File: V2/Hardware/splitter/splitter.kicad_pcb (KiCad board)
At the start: 2 copper layers, 19 parts, among them J0 Rpi_40Pin_F, J1 Control_seg:1, J2 Control_seg:2, J3 Control_seg:3, J4 Molex_PSU_F, J5 Siren, J6 USB_A_F, K0 RELRAS0515, Q0 BC548C, Q1 BD139-16

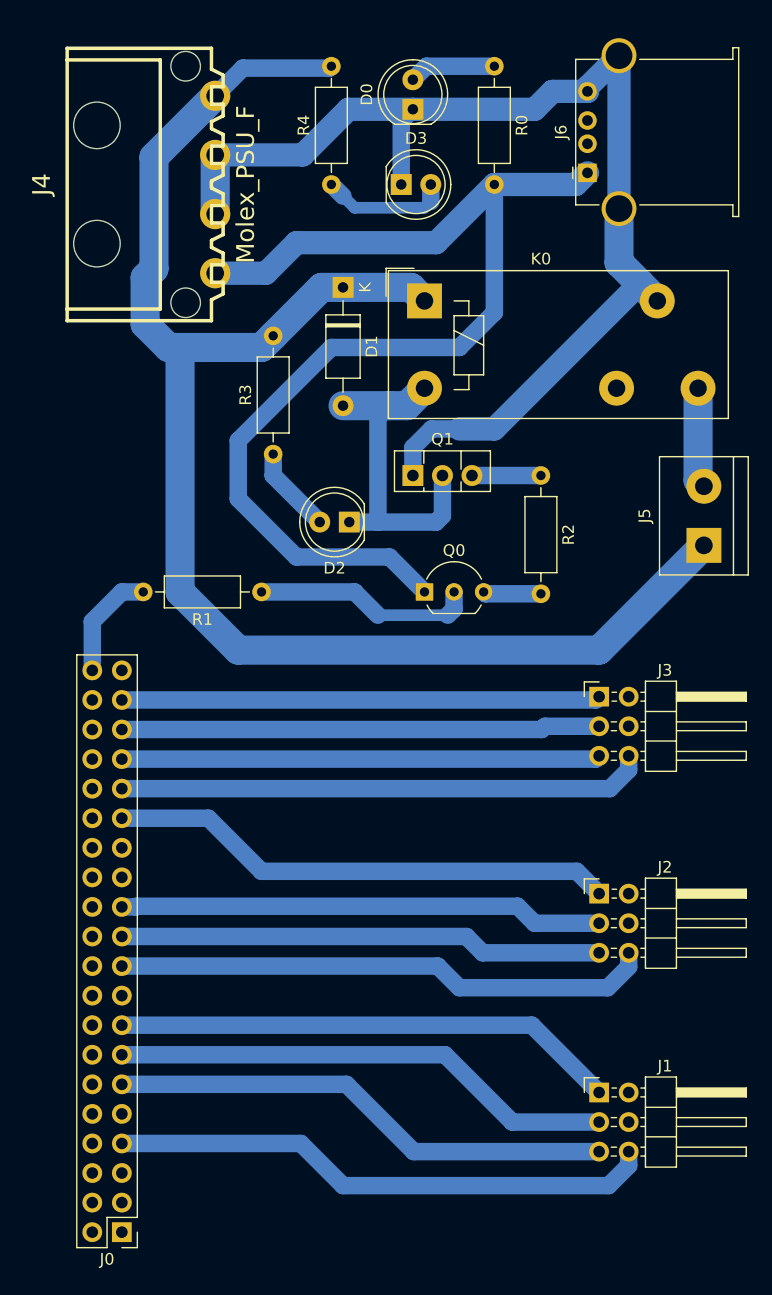
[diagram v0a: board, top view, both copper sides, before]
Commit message: Reinforce output
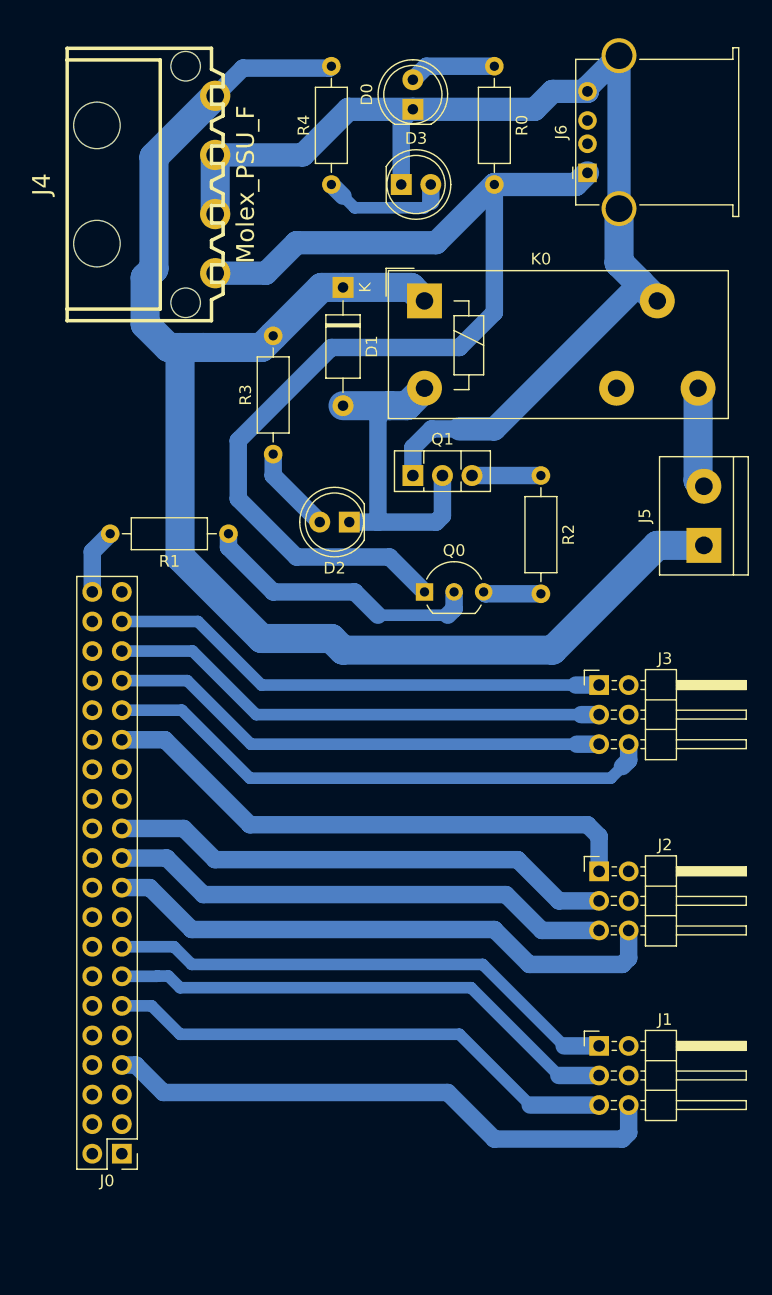
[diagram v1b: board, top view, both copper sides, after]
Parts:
- moved J0 6.74 mm to (124.0, 135.3)
- moved R1 5.75 mm to (133.2, 82.0)
- moved J1 4.00 mm to (165.0, 126.0)
- moved J2 1.92 mm to (165.0, 111.0)
- moved J3 1.00 mm to (165.0, 95.0)
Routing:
- net Net-(Q0-Pad2): track 19.1 -> 24.6 mm
- net /SIREN_gpio:21: track 9.63 -> 5.64 mm
- net /seg:2_bit:d_gpio:05: track 43.7 -> 47.4 mm
- net /seg:2_bit:a_gpio:10: track 46.3 -> 48.9 mm
- net /seg:3_bit:a_gpio:06: track 45.4 -> 48.0 mm
- net /seg:3_bit:c_gpio:19: track 41.1 -> 43.3 mm
- net /seg:3_bit:d_gpio:26: track 41.1 -> 43.3 mm
- net /seg:3_bit:b_gpio:13: track 41.1 -> 43.3 mm
- net /seg:2_bit:b_gpio:09: track 41.6 -> 43.6 mm
- net /seg:2_bit:c_gpio:11: track 41.6 -> 43.6 mm
- net /seg:1_bit:a_gpio:04: track 47.0 -> 48.8 mm
- net /12V+: track 132.4 -> 130.6 mm
- net /seg:1_bit:c_gpio:27: track 43.4 -> 44.5 mm
- net /seg:1_bit:b_gpio:17: track 43.4 -> 44.5 mm
- net /seg:1_bit:d_gpio:22: track 43.4 -> 44.5 mm
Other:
- board text added: "100mm"
- board text removed: "107mm"

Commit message: Export -pcbs
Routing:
- net /seg:3_bit:d_gpio:26: track 43.3 -> 45.7 mm
- net /seg:3_bit:c_gpio:19: track 43.3 -> 45.3 mm
- net (no net): vias 0 -> 7
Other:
- board text added: "RPI"
- board text added: "SEG1"
- board text added: "SEG2"
- board text added: "SEG3"
- board text added: "SIREN"

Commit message: Fix relay symbol
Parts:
- K0: footprint Relay_THT:Relay_SPDT_Finder_40.31 -> Relay_THT:Relay_SPDT_Finder_36.11
- R1: value 100k -> 33k
- moved D1 12.0 mm to (155.0, 59.8)
- moved K0 10.8 mm to (160.0, 66.0)
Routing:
- net /12V+: track 130.6 -> 188.7 mm
- net Net-(J5-Pad2): track 8.63 -> 38.9 mm
- net Net-(D1-Pad2): track 29.7 -> 48.0 mm
- net /5V+: track 97.4 -> 109.7 mm
- net Earth: track 100.6 -> 107.8 mm
- net Net-(K0-Pad12): track 0.00 -> 5.20 mm
- net Net-(Q0-Pad3): track 4.99 -> 7.18 mm
- net Net-(Q1-Pad3): track 5.92 -> 7.92 mm
- net /SIREN_gpio:21: track 5.64 -> 7.64 mm
- net Net-(D0-Pad2): track 7.48 -> 9.32 mm
- net Net-(Q0-Pad2): track 24.6 -> 26.3 mm
- net Net-(D2-Pad2): track 7.50 -> 8.68 mm
- net Net-(D3-Pad2): track 11.1 -> 11.6 mm
- net (no net): vias 7 -> 8

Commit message: Update splitter board
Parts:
- J0: footprint Connector_PinHeader_2.54mm:PinHeader_2x20_P2.54mm_Vertical -> Connector_IDC:IDC-Header_2x20_P2.54mm_Vertical
- moved Q1 10.0 mm to (149.0, 67.0), turned to 270 degrees
- moved R1 9.78 mm to (137.0, 73.0)
- moved Q0 9.30 mm to (152.0, 77.9), turned to 270 degrees
- moved R3 7.91 mm to (143.0, 70.0)
- moved D2 4.47 mm to (145.5, 77.0)
- moved J0 3.05 mm to (124.5, 132.3)
- moved R2 3.00 mm to (157.0, 77.0), turned to 0 degrees
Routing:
- net Earth: track 107.8 -> 95.9 mm
- net /12V+: track 188.7 -> 177.9 mm
- net Net-(Q0-Pad3): track 7.18 -> 17.6 mm
- net /SIREN_gpio:21: track 7.64 -> 16.4 mm
- net /5V+: track 109.7 -> 101.8 mm
- net /seg:3_bit:a_gpio:06: track 48.0 -> 51.9 mm
- net Net-(D1-Pad2): track 48.0 -> 44.8 mm
- net Net-(Q1-Pad3): track 7.92 -> 10.0 mm
- net /seg:3_bit:c_gpio:19: track 45.3 -> 44.0 mm
- net /seg:1_bit:d_gpio:22: track 44.5 -> 45.8 mm
- net /seg:3_bit:b_gpio:13: track 43.3 -> 44.0 mm
- net /seg:2_bit:c_gpio:11: track 43.6 -> 44.3 mm
- net /seg:2_bit:a_gpio:10: track 48.9 -> 49.6 mm
- net /seg:2_bit:b_gpio:09: track 43.6 -> 44.3 mm
- net /seg:1_bit:b_gpio:17: track 44.5 -> 45.2 mm
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
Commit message: Make more precise plots
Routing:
- net (no net): track 0.00 -> 4.00 mm
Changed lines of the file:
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@@
   (general
     (thickness 1.6)
-    (drawings 27)
-    (tracks 224)
+    (drawings 29)
+    (tracks 226)
     (zones 0)
     (modules 19)
@@
   )
   (setup
-    (last_trace_width 2)
+    (last_trace_width 0.25)
     (user_trace_width 1)
     (user_trace_width 1.5)
@@
     (visible_elements FFFFFF7F)
     (pcbplotparams
-      (layerselection 0x010fc_ffffffff)
+      (layerselection 0x00800_fffffffe)
       (usegerberextensions false)
       (usegerberattributes true)
       (usegerberadvancedattributes true)
       (creategerberjobfile true)
-      (excludeedgelayer true)
+      (excludeedgelayer false)
       (linewidth 0.100000)
       (plotframeref false)
@@
       (psnegative false)
       (psa4output false)
-      (plotreference true)
-      (plotvalue true)
+      (plotreference false)
+      (plotvalue false)
       (plotinvisibletext false)
-      (padsonsilk false)
+      (padsonsilk true)
       (subtractmaskfromsilk false)
-      (outputformat 1)
+      (outputformat 5)
       (mirror false)
       (drillshape 1)
@@
     (pad 3 thru_hole circle (at 0 2.54 180) (size 1.7 1.7) (drill 1) (layers *.Cu *.Mask)
       (net 9 "Net-(J0-Pad3)"))
-    (pad 1 thru_hole roundrect (at 0 0 180) (size 1.7 1.7) (drill 1) (layers *.Cu *.Mask) (roundrect_rratio 0.147059)
+    (pad 1 thru_hole roundrect (at 0 0 180) (size 1.7 1.7) (drill 1) (layers *.Cu *.Mask) (roundrect_rratio 0.1470588235294118)
       (net 7 "Net-(J0-Pad1)"))
     (model ${KISYS3DMOD}/Connector_IDC.3dshapes/IDC-Header_2x20_P2.54mm_Vertical.wrl
@@
     )
   )
+  (gr_line (start 141 132) (end 139 132) (layer Eco2.User) (width 0.25))
+  (gr_line (start 140 131) (end 140 133) (layer Eco2.User) (width 0.25))
   (gr_circle (center 136 54) (end 137 55) (layer Eco2.User) (width 0.15))
   (gr_circle (center 136 54) (end 137 53) (layer F.CrtYd) (width 0.05))
@@
   (via (at 160 41) (size 0.8) (drill 0.4) (layers F.Cu B.Cu) (net 0))
   (via (at 136 54) (size 0.8) (drill 0.4) (layers F.Cu B.Cu) (net 0))
+  (segment (start 140 131) (end 140 133) (width 0.25) (layer B.Cu) (net 0))
+  (segment (start 141 132) (end 139 132) (width 0.25) (layer B.Cu) (net 0))
   (segment (start 132.02 49.46) (end 132.02 54.54) (width 2.5) (layer B.Cu) (net 1))
   (segment (start 148 46.54) (end 149 45.54) (width 1.5) (layer B.Cu) (net 1))

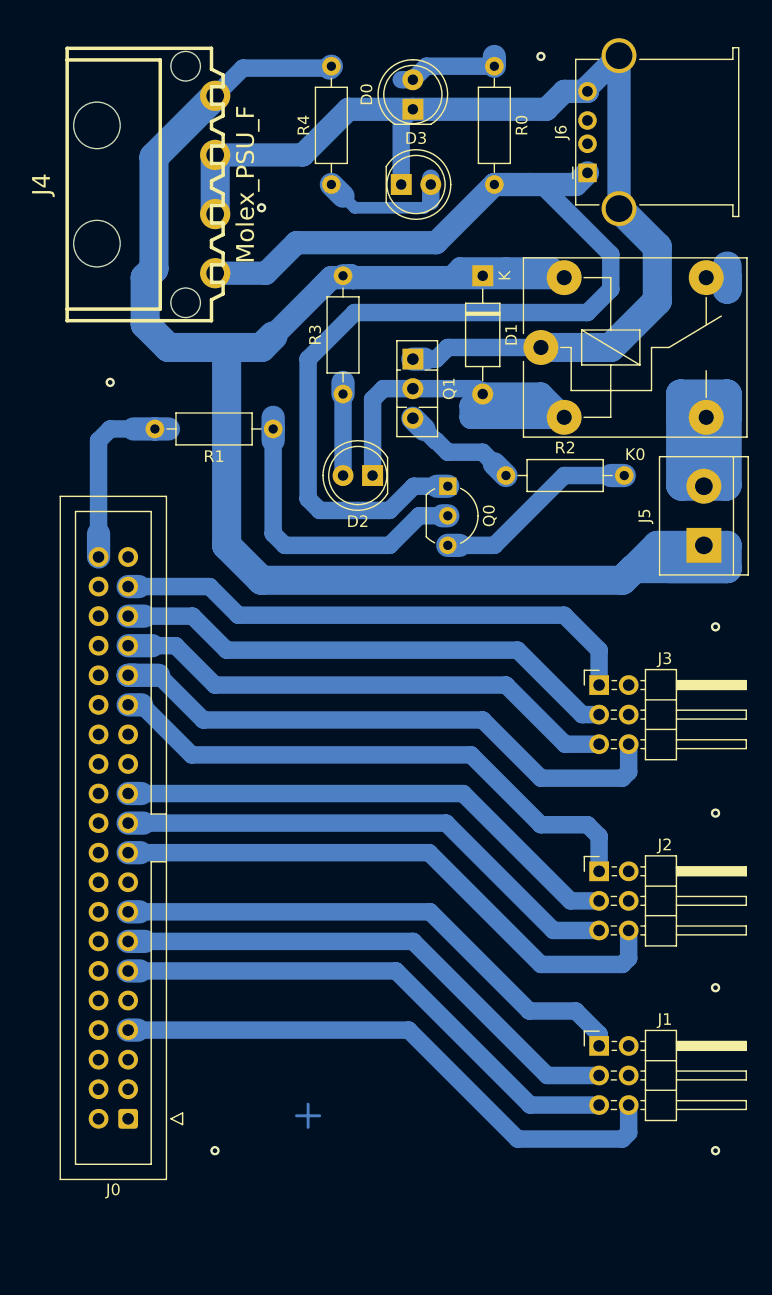
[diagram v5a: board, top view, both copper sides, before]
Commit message: Simplify relay control
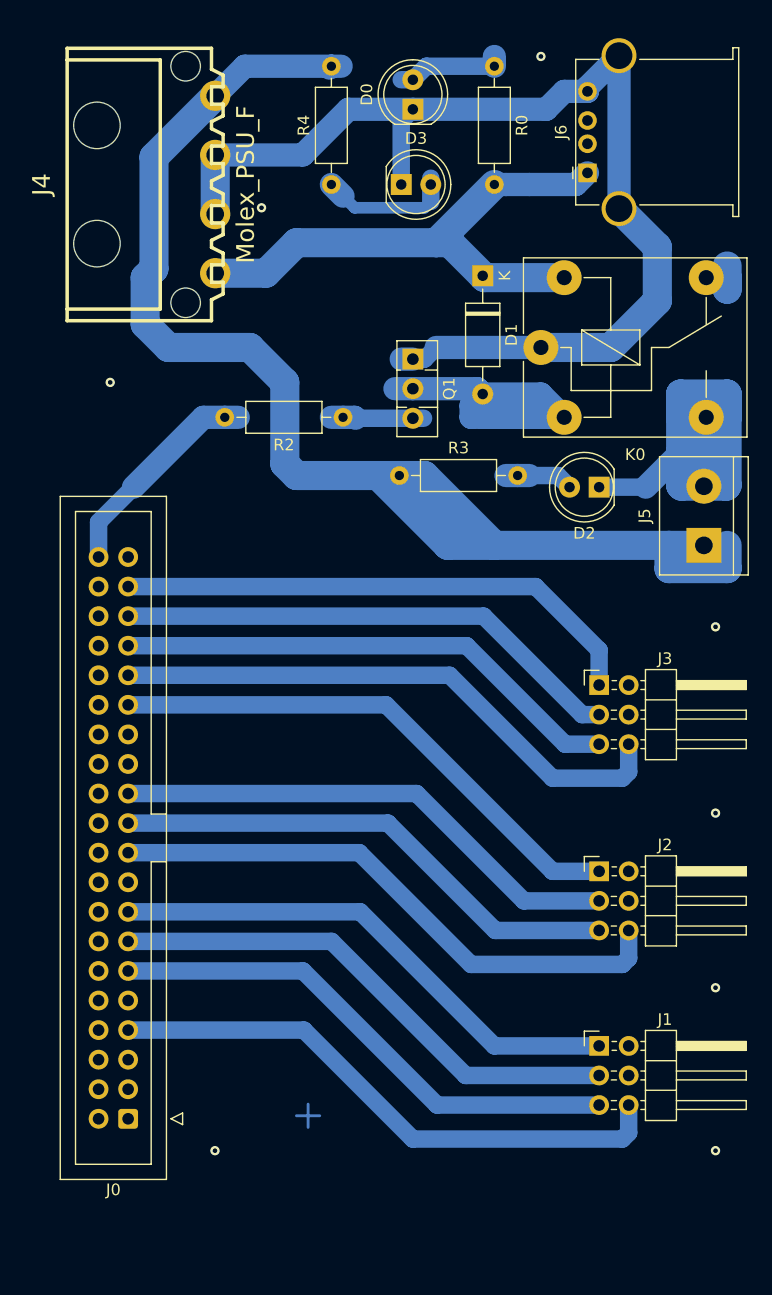
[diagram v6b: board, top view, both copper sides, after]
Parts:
- removed Q0: BC548C, Package_TO_SOT_THT:TO-92_Inline_Wide
- removed R1: 33k, Resistor_THT:R_Axial_DIN0207_L6.3mm_D2.5mm_P10.16mm_Horizontal
- moved D2 19.5 mm to (165.0, 78.0)
- moved R2 14.9 mm to (143.0, 72.0), turned to 180 degrees
- moved R3 8.51 mm to (147.8, 77.0), turned to 0 degrees
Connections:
- D1 pad 1: /12V+ -> /5V+
- D2 pad 1: Net-(D1-Pad2) -> Net-(D2-Pad1)
- J5 pad 2: Net-(J5-Pad2) -> Net-(D2-Pad1)
- K0 pad 14: Net-(J5-Pad2) -> Net-(D2-Pad1)
- K0 pad A1: /12V+ -> /5V+
- R2 pad 2: Net-(Q0-Pad3) -> /SIREN_gpio:21
- R3 pad 1: Net-(D2-Pad2) -> /12V+
- R3 pad 2: /12V+ -> Net-(D2-Pad2)
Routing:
- net /5V+: track 101.8 -> 47.8 mm
- net Net-(D2-Pad1): track 0.00 -> 47.1 mm
- net /12V+: track 177.9 -> 137.1 mm
- net Net-(J5-Pad2): track 38.9 -> 0.00 mm
- net Net-(Q0-Pad2): track 26.5 -> 0.00 mm
- net Net-(Q0-Pad3): track 17.6 -> 0.00 mm
- net Net-(D1-Pad2): track 44.8 -> 36.0 mm
- net /seg:3_bit:a_gpio:06: track 51.9 -> 49.3 mm
- net /SIREN_gpio:21: track 16.4 -> 18.7 mm
- net Net-(D2-Pad2): track 8.00 -> 5.87 mm
- net Net-(Q1-Pad3): track 10.0 -> 7.95 mm
- net /seg:2_bit:d_gpio:05: track 48.1 -> 46.4 mm
- net Earth: track 95.9 -> 96.9 mm
- net /seg:1_bit:d_gpio:22: track 45.8 -> 45.2 mm

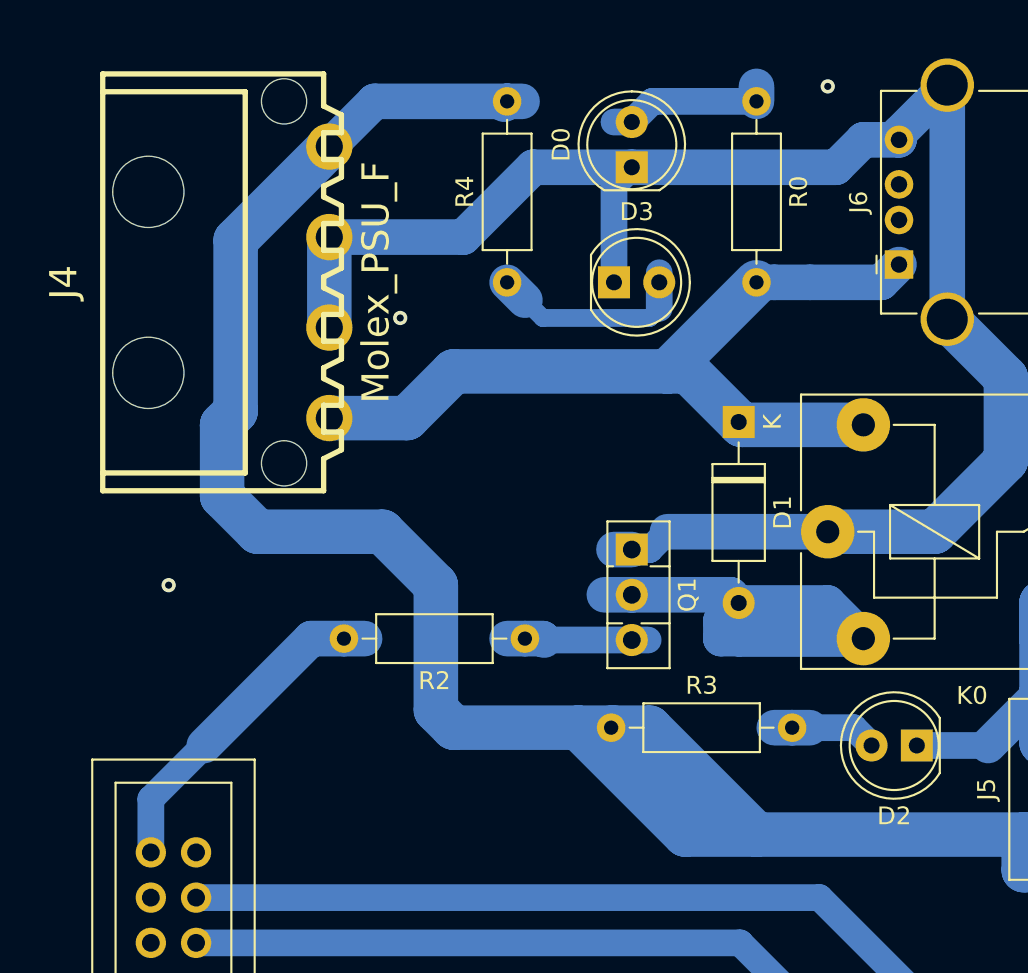
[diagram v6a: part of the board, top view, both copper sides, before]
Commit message: Add bypass caps and filtering
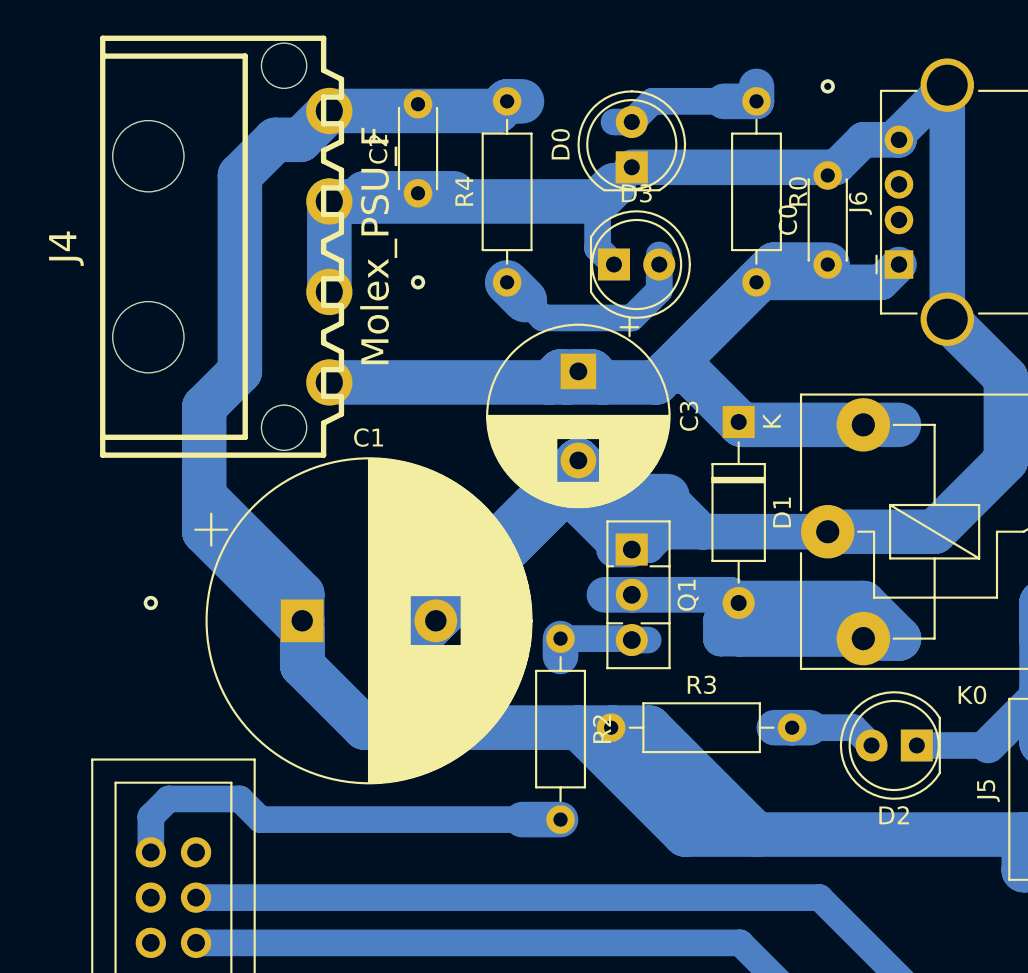
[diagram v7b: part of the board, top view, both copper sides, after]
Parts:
- added C0: 220nF, Capacitor_THT:C_Disc_D4.3mm_W1.9mm_P5.00mm, F.Cu at (160.0, 51.0)
- added C1: 4700uF 25V LOW ESR, Capacitor_THT:CP_Radial_D18.0mm_P7.50mm, F.Cu at (130.5, 71.0)
- added C2: 220nF, Capacitor_THT:C_Disc_D4.3mm_W1.9mm_P5.00mm, F.Cu at (137.0, 47.0)
- added C3: 100uF 25V LOW ESR, Capacitor_THT:CP_Radial_D10.0mm_P5.00mm, F.Cu at (146.0, 57.0)
- moved J4 2.00 mm to (126.0, 50.0)
- moved R2 2.00 mm to (145.0, 72.0), turned to 270 degrees
- moved D3 1.00 mm to (148.0, 51.0)
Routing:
- net Earth: track 96.9 -> 202.2 mm
- net /5V+: track 47.8 -> 57.8 mm
- net /SIREN_gpio:21: track 18.7 -> 25.9 mm
- net Net-(D1-Pad2): track 36.0 -> 40.0 mm
- net /12V+: track 137.1 -> 139.5 mm
- net Net-(Q1-Pad3): track 7.95 -> 5.95 mm

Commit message: More separation
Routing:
- net /12V+: track 139.5 -> 116.5 mm
